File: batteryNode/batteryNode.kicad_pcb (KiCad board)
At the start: 2 copper layers, 3 parts, among them U1 BQ76925RGER, U2 LTC2875-DD, U3 ATtiny2313A-MU

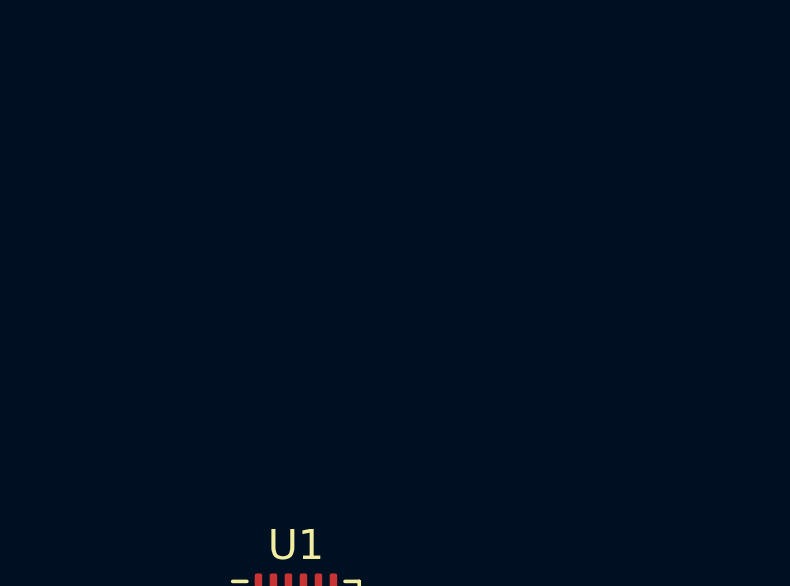
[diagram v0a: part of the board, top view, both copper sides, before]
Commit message: Added some footprints and digikey part numbers
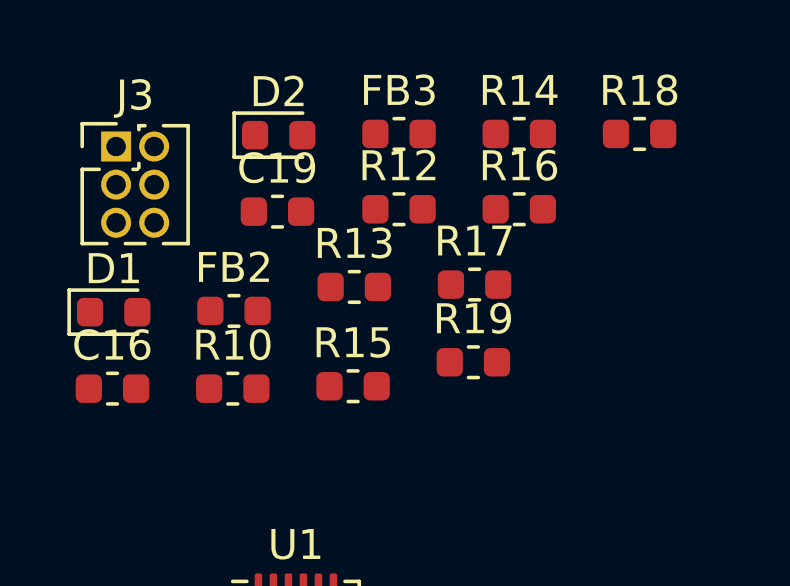
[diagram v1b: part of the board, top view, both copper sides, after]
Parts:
- added C16: 10n, Capacitor_SMD:C_0603_1608Metric, F.Cu at (30.7, 115.9)
- added C19: 10n, Capacitor_SMD:C_0603_1608Metric, F.Cu at (36.2, 110.0)
- added D1: LED, LED_SMD:LED_0603_1608Metric, F.Cu at (30.8, 113.4)
- added D2: LED, LED_SMD:LED_0603_1608Metric, F.Cu at (36.3, 107.5)
- added FB2: Ferrite, Inductor_SMD:L_0603_1608Metric, F.Cu at (34.8, 113.3)
- added FB3: Ferrite, Inductor_SMD:L_0603_1608Metric, F.Cu at (40.3, 107.4)
- added J3: ISP_Header, Connector_PinHeader_1.27mm:PinHeader_2x03_P1.27mm_Vertical, F.Cu at (30.8, 107.9)
- added R10: 1M, Capacitor_SMD:C_0603_1608Metric, F.Cu at (34.7, 115.9)
- added R12: 10k, Resistor_SMD:R_0603_1608Metric, F.Cu at (40.3, 109.9)
- added R13: 0, Resistor_SMD:R_0603_1608Metric, F.Cu at (38.8, 112.5)
- added R14: 10k, Resistor_SMD:R_0603_1608Metric, F.Cu at (44.3, 107.4)
- added R15: 10k, Resistor_SMD:R_0603_1608Metric, F.Cu at (38.7, 115.8)
- added R16: 0, Resistor_SMD:R_0603_1608Metric, F.Cu at (44.3, 109.9)
- added R17: 10k, Resistor_SMD:R_0603_1608Metric, F.Cu at (42.8, 112.5)
- added R18: 10k, Resistor_SMD:R_0603_1608Metric, F.Cu at (48.3, 107.4)
- added R19: 10k, Resistor_SMD:R_0603_1608Metric, F.Cu at (42.7, 115.0)
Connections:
- U3 pad 5: Net-(U3-Pad5) -> /iLED0
- U3 pad 6: Net-(U3-Pad6) -> /iLED1

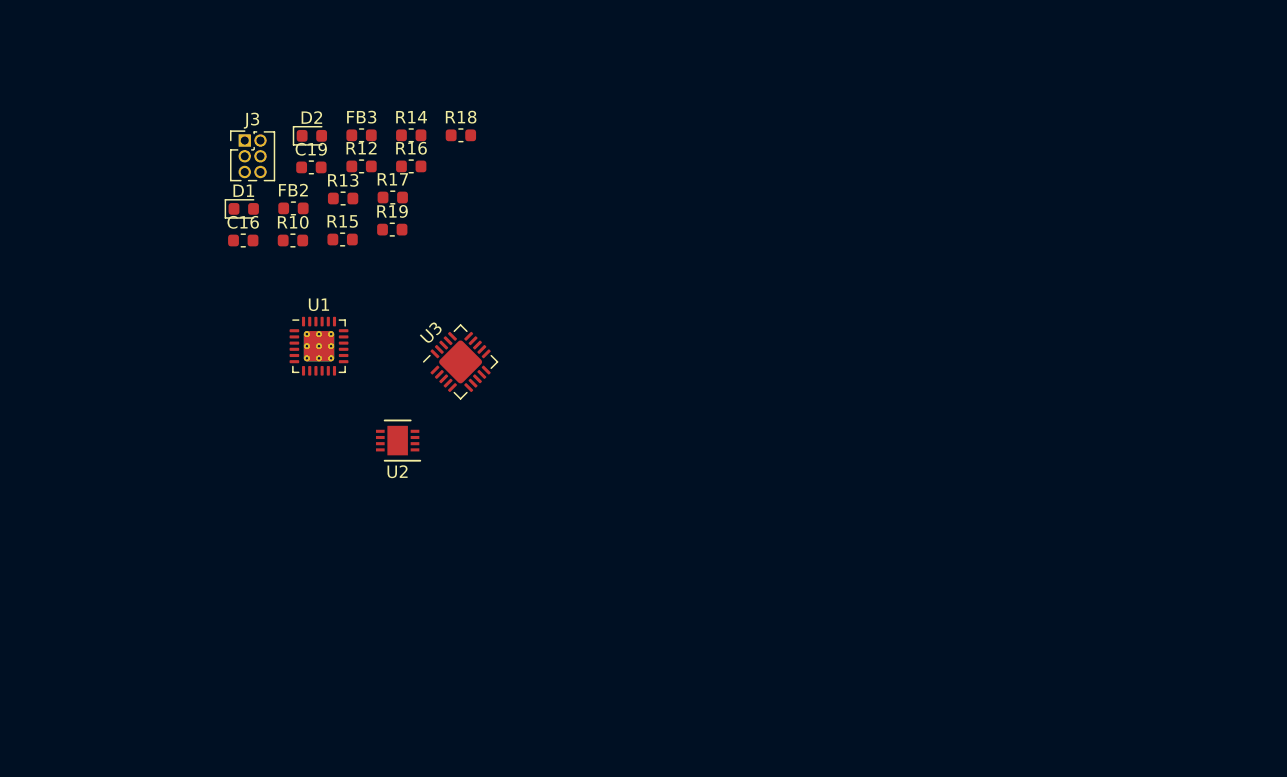
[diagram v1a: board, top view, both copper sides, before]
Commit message: Schematic Complete
V 0.1 of schematic complete. Trial layout next
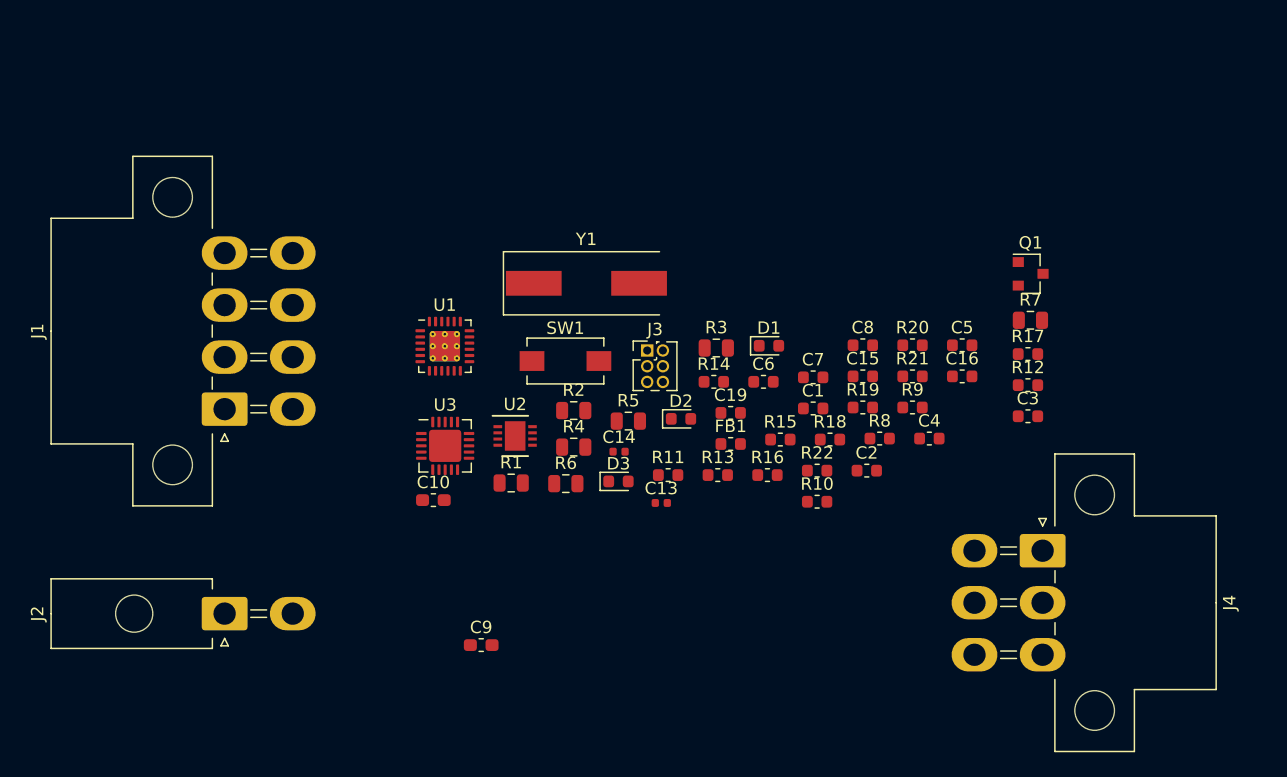
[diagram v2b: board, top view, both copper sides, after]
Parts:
- removed FB2, FB3: Ferrite, Inductor_SMD:L_0603_1608Metric
- added C1: 1u, Capacitor_SMD:C_0603_1608Metric, F.Cu at (76.7, 129.5)
- added C10: 4.7u, Capacitor_SMD:C_0603_1608Metric_Pad1.05x0.95mm_HandSolder, F.Cu at (46.1, 136.9)
- added C13: 20p, Capacitor_SMD:C_0402_1005Metric, F.Cu at (64.5, 137.1)
- added C14: 20p, Capacitor_SMD:C_0402_1005Metric, F.Cu at (61.1, 133.0)
- added C15: 1u, Capacitor_SMD:C_0603_1608Metric, F.Cu at (80.7, 126.9)
- added C2: 1u, Capacitor_SMD:C_0603_1608Metric, F.Cu at (81.1, 134.5)
- added C3: 1u, Capacitor_SMD:C_0603_1608Metric, F.Cu at (94.1, 130.1)
- added C4: 1u, Capacitor_SMD:C_0603_1608Metric, F.Cu at (86.1, 131.9)
- added C5: 1u, Capacitor_SMD:C_0603_1608Metric, F.Cu at (88.8, 124.4)
- added C6: 1u, Capacitor_SMD:C_0603_1608Metric, F.Cu at (72.7, 127.3)
- added C7: 1u, Capacitor_SMD:C_0603_1608Metric, F.Cu at (76.7, 127.0)
- added C8: 1u, Capacitor_SMD:C_0603_1608Metric, F.Cu at (80.7, 124.4)
- added C9: 10u, Capacitor_SMD:C_0603_1608Metric_Pad1.05x0.95mm_HandSolder, F.Cu at (49.9, 148.6)
- added D3: LED, LED_SMD:LED_0603_1608Metric, F.Cu at (61.0, 135.4)
- added FB1: Ferrite, Inductor_SMD:L_0603_1608Metric, F.Cu at (70.1, 132.4)
- added J1: cell_taps, Connector_Molex:Molex_Mini-Fit_Jr_5569-08A1_2x04_P4.20mm_Horizontal, F.Cu at (29.2, 129.5)
- added J2: therm_conn, Connector_Molex:Molex_Mini-Fit_Jr_5569-02A2_2x01_P4.20mm_Horizontal, F.Cu at (29.2, 146.1)
- added J4: Conn_01x06, Connector_Molex:Molex_Mini-Fit_Jr_5569-06A1_2x03_P4.20mm_Horizontal, F.Cu at (95.2, 141.0)
- added Q1: IRLML9303TRPBF, Package_TO_SOT_SMD:SOT-23, F.Cu at (94.3, 118.6)
- added R1: 75, Resistor_SMD:R_0805_2012Metric, F.Cu at (52.3, 135.5)
- added R11: 120, Resistor_SMD:R_0603_1608Metric, F.Cu at (65.0, 134.9)
- added R2: 75, Resistor_SMD:R_0805_2012Metric, F.Cu at (57.4, 129.7)
- added R20: 0, Resistor_SMD:R_0603_1608Metric, F.Cu at (84.7, 124.4)
- added R21: 200k, Resistor_SMD:R_0603_1608Metric, F.Cu at (84.7, 126.9)
- added R22: 10k, Resistor_SMD:R_0603_1608Metric, F.Cu at (77.0, 134.5)
- added R3: 75, Resistor_SMD:R_0805_2012Metric, F.Cu at (68.9, 124.6)
- added R4: 75, Resistor_SMD:R_0805_2012Metric, F.Cu at (57.4, 132.6)
- added R5: 75, Resistor_SMD:R_0805_2012Metric, F.Cu at (61.8, 130.5)
- added R6: 75, Resistor_SMD:R_0805_2012Metric, F.Cu at (56.8, 135.6)
- added R7: 75, Resistor_SMD:R_0805_2012Metric, F.Cu at (94.3, 122.4)
- added R8: R, Resistor_SMD:R_0603_1608Metric, F.Cu at (82.1, 131.9)
- added R9: R, Resistor_SMD:R_0603_1608Metric, F.Cu at (84.7, 129.4)
- added SW1: SW_Push, Button_Switch_SMD:SW_SPST_EVQPE1, F.Cu at (56.7, 125.7)
- added Y1: 8MHz, Crystal:Crystal_SMD_HC49-SD, F.Cu at (58.4, 119.4)
- C16, C19: value 10n -> .1u
- moved C16 59.1 mm to (88.8, 126.9)
- moved R12 56.6 mm to (94.1, 127.6)
- moved R17 52.8 mm to (94.1, 125.1)
- moved R10 47.3 mm to (77.0, 137.0)
- moved D1 43.8 mm to (73.2, 124.4)
- moved R19 40.6 mm to (80.7, 129.4)
- moved C19 39.2 mm to (70.1, 129.8)
- moved R15 38.9 mm to (74.1, 132.0)
- moved R18 38.6 mm to (78.1, 132.0)
- moved R16 38.1 mm to (73.0, 134.9)
- moved R13 37.6 mm to (69.0, 134.9)
- moved D2 37.6 mm to (66.1, 130.3)
- moved J3 36.6 mm to (63.3, 124.8)
- moved R14 31.5 mm to (68.7, 127.3)
- moved U1 10.2 mm to (47.0, 124.5)
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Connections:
- C16 pad 1: Net-(C16-Pad1) -> /therm_in_filt
- C19 pad 1: Net-(C19-Pad1) -> /v_cell_filt
- R13 pad 1: Net-(C16-Pad1) -> /therm_in_filt
- R16 pad 1: Net-(C19-Pad1) -> /v_cell_filt
- U1 pad 23: /tap6 -> /v_ctl
- U1 pad 24: /tap6 -> /v_batt_filt

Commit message: Terrible First Version Layout
First version layout. Going to try some routing with this and see how it works out.
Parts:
- removed C1, C15, C2, C3, C4, C5, C6, C7, C8: 1u, Capacitor_SMD:C_0603_1608Metric
- removed C10: 4.7u, Capacitor_SMD:C_0603_1608Metric_Pad1.05x0.95mm_HandSolder
- removed C13, C14: 20p, Capacitor_SMD:C_0402_1005Metric
- removed C16, C19: .1u, Capacitor_SMD:C_0603_1608Metric
- removed C9: 10u, Capacitor_SMD:C_0603_1608Metric_Pad1.05x0.95mm_HandSolder
- removed D1, D2, D3: LED, LED_SMD:LED_0603_1608Metric
- removed FB1: Ferrite, Inductor_SMD:L_0603_1608Metric
- removed J1: cell_taps, Connector_Molex:Molex_Mini-Fit_Jr_5569-08A1_2x04_P4.20mm_Horizontal
- removed J2: therm_conn, Connector_Molex:Molex_Mini-Fit_Jr_5569-02A2_2x01_P4.20mm_Horizontal
- removed J3: ISP_Header, Connector_PinHeader_1.27mm:PinHeader_2x03_P1.27mm_Vertical
- removed J4: Conn_01x06, Connector_Molex:Molex_Mini-Fit_Jr_5569-06A1_2x03_P4.20mm_Horizontal
- removed Q1: IRLML9303TRPBF, Package_TO_SOT_SMD:SOT-23
- removed R1, R2, R3, R4, R5, R6, R7: 75, Resistor_SMD:R_0805_2012Metric
- removed R10: 1M, Capacitor_SMD:C_0603_1608Metric
- removed R11: 120, Resistor_SMD:R_0603_1608Metric
- removed R12, R14, R15, R17, R18, R19, R22: 10k, Resistor_SMD:R_0603_1608Metric
- removed R13, R16, R20: 0, Resistor_SMD:R_0603_1608Metric
- removed R21: 200k, Resistor_SMD:R_0603_1608Metric
- removed R8, R9: R, Resistor_SMD:R_0603_1608Metric
- removed SW1: SW_Push, Button_Switch_SMD:SW_SPST_EVQPE1
- removed U1: BQ76925RGER, Package_DFN_QFN:VQFN-24-1EP_4x4mm_P0.5mm_EP2.45x2.45mm_ThermalVias
- removed U2: LTC2875-DD, Package_DFN_QFN:DFN-8-1EP_3x3mm_P0.5mm_EP1.66x2.38mm
- removed U3: ATtiny2313A-MU, Package_DFN_QFN:MLF-20-1EP_4x4mm_P0.5mm_EP2.6x2.6mm
- removed Y1: 8MHz, Crystal:Crystal_SMD_HC49-SD
- added C101: 1u, Capacitor_SMD:C_0603_1608Metric, F.Cu at (72.5, 123.2)
- added C102: 1u, Capacitor_SMD:C_0603_1608Metric, F.Cu at (72.6, 118.6)
- added C103: 1u, Capacitor_SMD:C_0603_1608Metric, F.Cu at (72.5, 113.9)
- added C104: 1u, Capacitor_SMD:C_0603_1608Metric, F.Cu at (68.1, 125.2)
- added C105: 1u, Capacitor_SMD:C_0603_1608Metric, F.Cu at (68.1, 121.0)
- added C106: 1u, Capacitor_SMD:C_0603_1608Metric, F.Cu at (68.2, 116.7)
- added C107: 1u, Capacitor_SMD:C_0603_1608Metric, F.Cu at (68.1, 112.4)
- added C108: 10u, Capacitor_SMD:C_0603_1608Metric_Pad1.05x0.95mm_HandSolder, F.Cu at (72.5, 110.4)
- added C109: 4.7u, Capacitor_SMD:C_0603_1608Metric_Pad1.05x0.95mm_HandSolder, F.Cu at (82.9, 113.4)
- added C200: 1u, Capacitor_SMD:C_0603_1608Metric, F.Cu at (88.3, 111.6)
- added C201: 18p, Capacitor_SMD:C_0402_1005Metric, F.Cu at (98.8, 104.8)
- added C202: 18p, Capacitor_SMD:C_0402_1005Metric, F.Cu at (94.7, 104.9)
- added C203: .1u, Capacitor_SMD:C_0603_1608Metric, F.Cu at (82.4, 107.4)
- added C204: .1u, Capacitor_SMD:C_0603_1608Metric, F.Cu at (79.1, 105.5)
- added C300: 1u, Capacitor_SMD:C_0603_1608Metric, F.Cu at (93.0, 111.4)
- added D10: LED, LED_SMD:LED_0603_1608Metric, F.Cu at (85.6, 117.3)
- added D200: LED, LED_SMD:LED_0603_1608Metric, F.Cu at (103.4, 103.7)
- added D201: LED, LED_SMD:LED_0603_1608Metric, F.Cu at (104.9, 111.3)
- added FB300: Ferrite, Inductor_SMD:L_0603_1608Metric, F.Cu at (86.1, 126.9)
- added J100: cell_taps, Connector_Molex:Molex_Mini-Fit_Jr_5569-08A2_2x04_P4.20mm_Horizontal, F.Cu at (55.9, 127.0)
- added J101: therm_conn, Connector_Molex:Molex_Mini-Fit_Jr_5569-02A2_2x01_P4.20mm_Horizontal, F.Cu at (55.9, 106.7)
- added J200: ISP_Header, Connector_PinHeader_1.27mm:PinHeader_2x03_P1.27mm_Vertical, F.Cu at (81.7, 125.3)
- added J300: Conn_01x06, Connector_Molex:Molex_Mini-Fit_Jr_5569-06A2_2x03_P4.20mm_Horizontal, F.Cu at (96.8, 118.5)
- added Q100: IRLML9303TRPBF, Package_TO_SOT_SMD:SOT-23, F.Cu at (79.2, 113.5)
- added R101: 75, Resistor_SMD:R_0805_2012Metric, F.Cu at (68.1, 114.4)
- added R102: 75, Resistor_SMD:R_0805_2012Metric, F.Cu at (68.1, 118.5)
- added R103: 75, Resistor_SMD:R_0805_2012Metric, F.Cu at (68.1, 122.8)
- added R104: 75, Resistor_SMD:R_0805_2012Metric, F.Cu at (68.1, 127.0)
- added R105: 75, Resistor_SMD:R_0805_2012Metric, F.Cu at (72.6, 115.8)
- added R106: 75, Resistor_SMD:R_0805_2012Metric, F.Cu at (72.6, 120.5)
- added R107: 75, Resistor_SMD:R_0805_2012Metric, F.Cu at (72.5, 124.8)
- added R108: 0, Resistor_SMD:R_0603_1608Metric, F.Cu at (72.5, 112.0)
- added R109: 200k, Resistor_SMD:R_0603_1608Metric, F.Cu at (79.1, 111.1)
- added R110: 10k, Resistor_SMD:R_0603_1608Metric, F.Cu at (83.8, 115.8)
- added R200: 10k, Resistor_SMD:R_0603_1608Metric, F.Cu at (89.8, 111.6)
- added R201: 10k, Resistor_SMD:R_0603_1608Metric, F.Cu at (85.2, 111.6)
- added R202: 10k, Resistor_SMD:R_0603_1608Metric, F.Cu at (86.7, 111.6)
- added R203: 10k, Resistor_SMD:R_0603_1608Metric, F.Cu at (91.6, 106.6)
- added R204: 1M, Capacitor_SMD:C_0603_1608Metric, F.Cu at (96.8, 105.0)
- added R205: 10k, Resistor_SMD:R_0603_1608Metric, F.Cu at (103.4, 105.2)
- added R206: 10k, Resistor_SMD:R_0603_1608Metric, F.Cu at (104.9, 112.8)
- added R207: 0, Resistor_SMD:R_0603_1608Metric, F.Cu at (82.4, 109.1)
- added R208: 0, Resistor_SMD:R_0603_1608Metric, F.Cu at (77.6, 105.5)
- added R300: R, Resistor_SMD:R_0603_1608Metric, F.Cu at (102.4, 107.4)
- added R301: R, Resistor_SMD:R_0603_1608Metric, F.Cu at (102.4, 109.0)
- added R302: 120, Resistor_SMD:R_0603_1608Metric, F.Cu at (101.6, 111.4)
- added SW200: SW_Push, Button_Switch_SMD:SW_SPST_EVQPE1, F.Cu at (69.6, 105.3)
- added U100: BQ76925RGER, Package_DFN_QFN:VQFN-24-1EP_4x4mm_P0.5mm_EP2.45x2.45mm_ThermalVias, F.Cu at (80.1, 119.5)
- added U200: ATtiny2313A-MU, Package_DFN_QFN:MLF-20-1EP_4x4mm_P0.5mm_EP2.6x2.6mm, F.Cu at (87.2, 107.3)
- added U300: LTC2875-DD, Package_DFN_QFN:DFN-8-1EP_3x3mm_P0.5mm_EP1.66x2.38mm, F.Cu at (96.6, 111.4)
- added Y200: 10MHz, BMSLib:ECS-100-18-23G-JGN-TR, F.Cu at (93.6, 107.2)
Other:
- board outline added: 62 x 37.9 mm

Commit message: Made some small changes
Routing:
- net Net-(J100-Pad2): track 0.00 -> 21.6 mm
- net /tap4: track 0.00 -> 14.8 mm
- net +3V3: track 0.00 -> 8.83 mm
- net GND: track 0.00 -> 6.92 mm
- net Net-(D10-Pad2): track 0.00 -> 1.61 mm
- net /v_batt_filt: track 0.00 -> 0.53 mm
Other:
- board size 62 x 37.9 mm -> 62.2 x 27.9 mm
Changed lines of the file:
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@@
   (general
     (thickness 1.6)
-    (drawings 8)
-    (tracks 0)
+    (drawings 4)
+    (tracks 30)
     (zones 0)
     (modules 51)
@@
       (net 29 "Net-(C202-Pad1)"))
   )
-  (gr_arc (start 105.41 134.62) (end 104.140001 135.889999) (angle -180) (layer Edge.Cuts) (width 0.05))
-  (gr_arc (start 46.99 134.62) (end 45.720001 133.350001) (angle -180) (layer Edge.Cuts) (width 0.05))
-  (gr_arc (start 46.99 100.33) (end 48.259999 99.060001) (angle -180) (layer Edge.Cuts) (width 0.05))
-  (gr_arc (start 105.41 100.33) (end 106.679999 101.599999) (angle -180) (layer Edge.Cuts) (width 0.05))
-  (gr_line (start 106.68 133.35) (end 106.68 101.6) (layer Edge.Cuts) (width 0.05))
-  (gr_line (start 48.26 135.89) (end 104.14 135.89) (layer Edge.Cuts) (width 0.05))
-  (gr_line (start 48.26 99.06) (end 104.14 99.06) (layer Edge.Cuts) (width 0.05))
-  (gr_line (start 45.72 101.6) (end 45.720001 133.350001) (layer Edge.Cuts) (width 0.05))
+  (gr_line (start 45.72 130.81) (end 107.95 130.81) (layer Edge.Cuts) (width 0.05))
+  (gr_line (start 45.72 102.87) (end 45.72 130.81) (layer Edge.Cuts) (width 0.05))
+  (gr_line (start 107.95 102.87) (end 45.72 102.87) (layer Edge.Cuts) (width 0.05))
+  (gr_line (start 107.95 130.81) (end 107.95 102.87) (layer Edge.Cuts) (width 0.05))
+  (segment (start 67.2845 121.606) (end 67.2845 121.031) (width 0.25) (layer F.Cu) (net 3))
+  (segment (start 67.2845 122.58835) (end 67.2845 121.606) (width 0.25) (layer F.Cu) (net 3))
+  (segment (start 69.48884 123.83401) (end 68.53016 123.83401) (width 0.25) (layer F.Cu) (net 3))
+  (segment (start 70.93286 122.38999) (end 69.48884 123.83401) (width 0.25) (layer F.Cu) (net 3))
+  (segment (start 68.53016 123.83401) (end 67.2845 122.58835) (width 0.25) (layer F.Cu) (net 3))
+  (segment (start 74.52901 122.38999) (end 70.93286 122.38999) (width 0.25) (layer F.Cu) (net 3))
+  (segment (start 77.662 119.257) (end 74.52901 122.38999) (width 0.25) (layer F.Cu) (net 3))
+  (segment (start 78.1495 119.257) (end 77.662 119.257) (width 0.25) (layer F.Cu) (net 3))
+  (segment (start 78.69129 121.69021) (end 76.42979 121.69021) (width 0.25) (layer F.Cu) (net 7))
+  (segment (start 78.887 121.4945) (end 78.69129 121.69021) (width 0.25) (layer F.Cu) (net 7))
+  (segment (start 76.42979 121.86571) (end 73.4545 124.841) (width 0.25) (layer F.Cu) (net 7))
+  (segment (start 76.42979 121.69021) (end 76.42979 121.86571) (width 0.25) (layer F.Cu) (net 7))
+  (segment (start 83.0325 115.824) (end 81.534 115.824) (width 0.25) (layer F.Cu) (net 13))
+  (segment (start 80.887 116.471) (end 80.887 117.5195) (width 0.25) (layer F.Cu) (net 13))
+  (segment (start 81.534 115.824) (end 80.887 116.471) (width 0.25) (layer F.Cu) (net 13))
+  (segment (start 82.931 115.7225) (end 83.0325 115.824) (width 0.25) (layer F.Cu) (net 13))
+  (segment (start 82.931 114.286) (end 82.931 115.7225) (width 0.25) (layer F.Cu) (net 13))
+  (segment (start 79.5 114.286) (end 79.248 114.538) (width 0.25) (layer F.Cu) (net 13))
+  (segment (start 82.931 114.286) (end 79.5 114.286) (width 0.25) (layer F.Cu) (net 13))
+  (segment (start 78.887 117.5195) (end 78.887 116.987) (width 0.25) (layer F.Cu) (net 25))
+  (segment (start 84.8105 116.027) (end 84.6075 115.824) (width 0.25) (layer F.Cu) (net 30))
+  (segment (start 84.8105 117.348) (end 84.8105 116.027) (width 0.25) (layer F.Cu) (net 30))
+  (segment (start 68.83884 128.67501) (end 60.09501 128.67501) (width 0.25) (layer F.Cu) (net 35))
+  (segment (start 71.023263 126.490587) (end 68.83884 128.67501) (width 0.25) (layer F.Cu) (net 35))
+  (segment (start 71.5795 124.841) (end 71.023263 125.397237) (width 0.25) (layer F.Cu) (net 35))
+  (segment (start 71.023263 125.397237) (end 71.023263 126.490587) (width 0.25) (layer F.Cu) (net 35))
+  (segment (start 56.38 122.8) (end 55.88 122.8) (width 0.25) (layer F.Cu) (net 35))
+  (segment (start 59.20499 125.62499) (end 56.38 122.8) (width 0.25) (layer F.Cu) (net 35))
+  (segment (start 59.20499 127.78499) (end 59.20499 125.62499) (width 0.25) (layer F.Cu) (net 35))
+  (segment (start 60.09501 128.67501) (end 59.20499 127.78499) (width 0.25) (layer F.Cu) (net 35))
 )
